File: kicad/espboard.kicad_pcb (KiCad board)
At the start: 2 copper layers, 48.3 x 40.6 mm, 14 parts, among them P1 CONN_PWR, P2 CONN_UART, P3 CONN_IO, SW1 SW_RST, SW2 SW_FLASH, U1 ESP-01v090, U2 LM1117-3.3

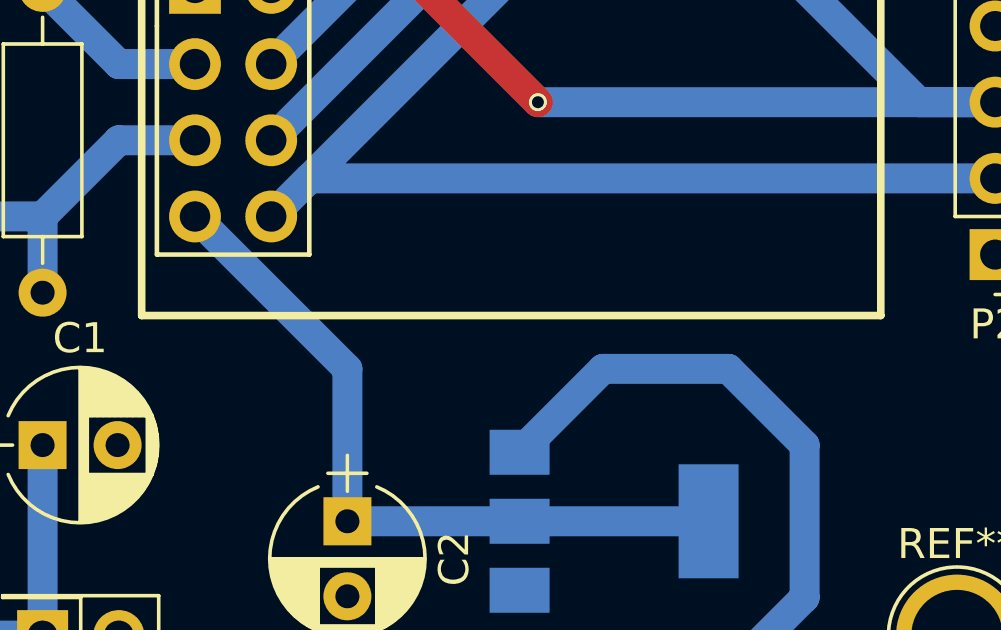
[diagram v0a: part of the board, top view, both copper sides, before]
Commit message: Fix plan de masse et ajout texte
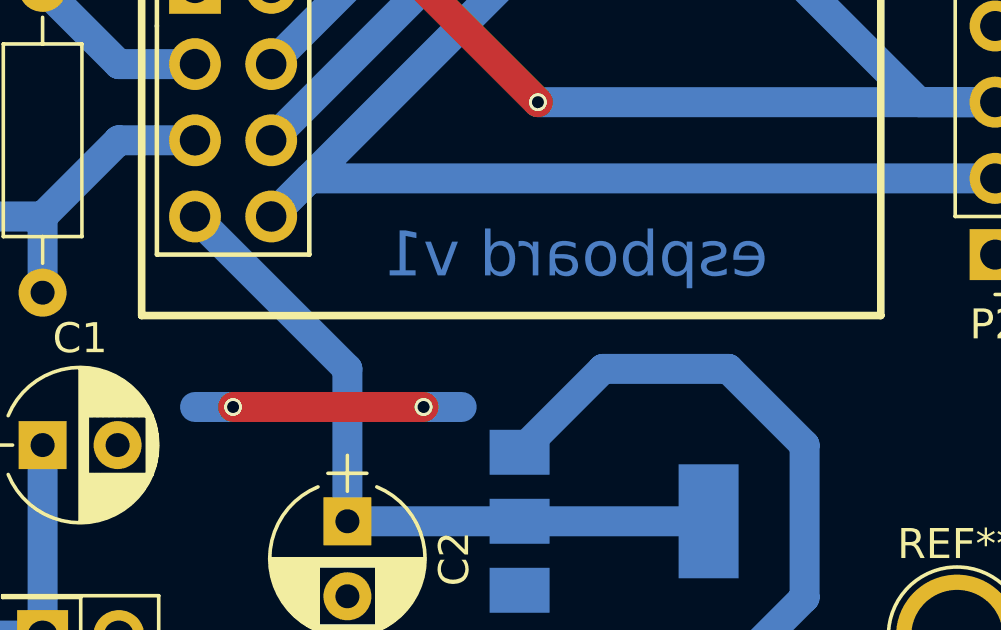
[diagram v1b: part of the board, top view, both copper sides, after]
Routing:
- net GND: track 9.78 -> 18.7 mm, vias 0 -> 2
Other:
- board text added: "espboard v1"
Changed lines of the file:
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@@
   (general
     (links 31)
-    (no_connects 2)
-    (area 130.734999 104.064999 179.145001 143.585001)
+    (no_connects 1)
+    (area 130.734999 102.794999 179.145001 143.585001)
     (thickness 1.6)
-    (drawings 6)
-    (tracks 58)
+    (drawings 7)
+    (tracks 63)
     (zones 0)
     (modules 14)
@@
       (effects (font (size 1 1) (thickness 0.15)))
     )
-    (fp_text value CONN_UART (at 0 12.49 180) (layer F.Fab)
+    (fp_text value CONN_UART (at 0 -6.35 270) (layer F.Fab)
       (effects (font (size 1 1) (thickness 0.15)))
     )
@@
       (effects (font (size 1 1) (thickness 0.15)))
     )
-    (fp_text value SW_RST (at 3.75 6.7 270) (layer F.Fab)
+    (fp_text value SW_RST (at 3.81 -2.54 270) (layer F.Fab)
       (effects (font (size 1 1) (thickness 0.15)))
     )
@@
     (fp_circle (center 0 0) (end 0 -2.286) (layer F.SilkS) (width 0.12))
     (pad 1 thru_hole circle (at 0 0) (size 4.064 4.064) (drill 3.048) (layers *.Cu *.Mask))
+  )
+  (gr_text "espboard v1" (at 162.56 127) (layer B.Cu)
+    (effects (font (size 1.5 1.5) (thickness 0.3)) (justify mirror))
   )
   (gr_line (start 130.81 102.87) (end 130.81 104.14) (angle 90) (layer Edge.Cuts) (width 0.15))
@@
   (segment (start 144.78 140.97) (end 146.05 142.24) (width 1) (layer B.Cu) (net 1))
   (segment (start 144.78 139.7) (end 144.78 133.35) (width 1) (layer B.Cu) (net 1))
+  (segment (start 149.86 132.08) (end 151.13 132.08) (width 1) (layer B.Cu) (net 2))
+  (segment (start 157.48 132.08) (end 158.75 132.08) (width 1) (layer B.Cu) (net 2))
+  (via (at 157.48 132.08) (size 0.6) (drill 0.4) (layers F.Cu B.Cu) (net 2))
+  (segment (start 151.13 132.08) (end 157.48 132.08) (width 1) (layer F.Cu) (net 2))
+  (via (at 151.13 132.08) (size 0.6) (drill 0.4) (layers F.Cu B.Cu) (net 2))
   (segment (start 152.4 118.11) (end 157.48 113.03) (width 1) (layer B.Cu) (net 2))
   (segment (start 157.48 113.03) (end 157.48 110.49) (width 1) (layer B.Cu) (net 2))

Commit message: Finalize PCB sheet
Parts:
- moved P2 68.2 mm to (115.6, 96.5)
- moved R1 68.2 mm to (83.8, 97.8)
- moved REF** 68.2 mm to (73.7, 76.2)
- moved SW1 68.2 mm to (77.5, 95.2)
- moved SW2 68.2 mm to (73.0, 89.5)
- moved U1 68.2 mm to (88.9, 87.6)
- moved C1 68.2 mm to (83.8, 102.9)
- moved C2 68.2 mm to (94.0, 105.4)
- moved P1 68.2 mm to (83.8, 109.2)
- moved P3 68.2 mm to (88.9, 80.0)
- moved REF** 68.2 mm to (114.3, 76.2)
- moved REF** 68.2 mm to (114.3, 109.2)
- moved REF** 68.2 mm to (73.7, 109.2)
- moved U2 68.2 mm to (102.9, 105.4)
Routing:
- net (no net): track 0.00 -> 8.89 mm, vias 0 -> 2
- net GND: track 18.7 -> 9.78 mm, vias 2 -> 0

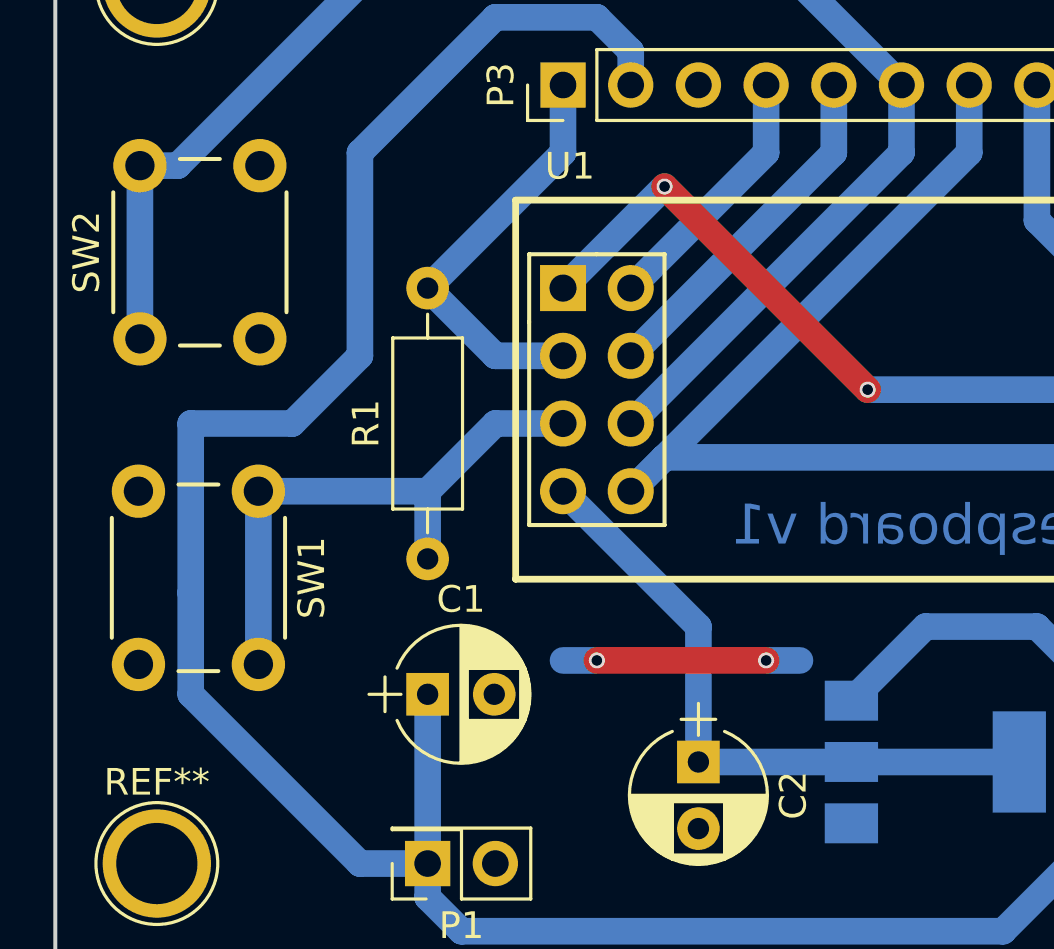
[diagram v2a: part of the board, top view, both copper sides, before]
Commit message: Bigger vias
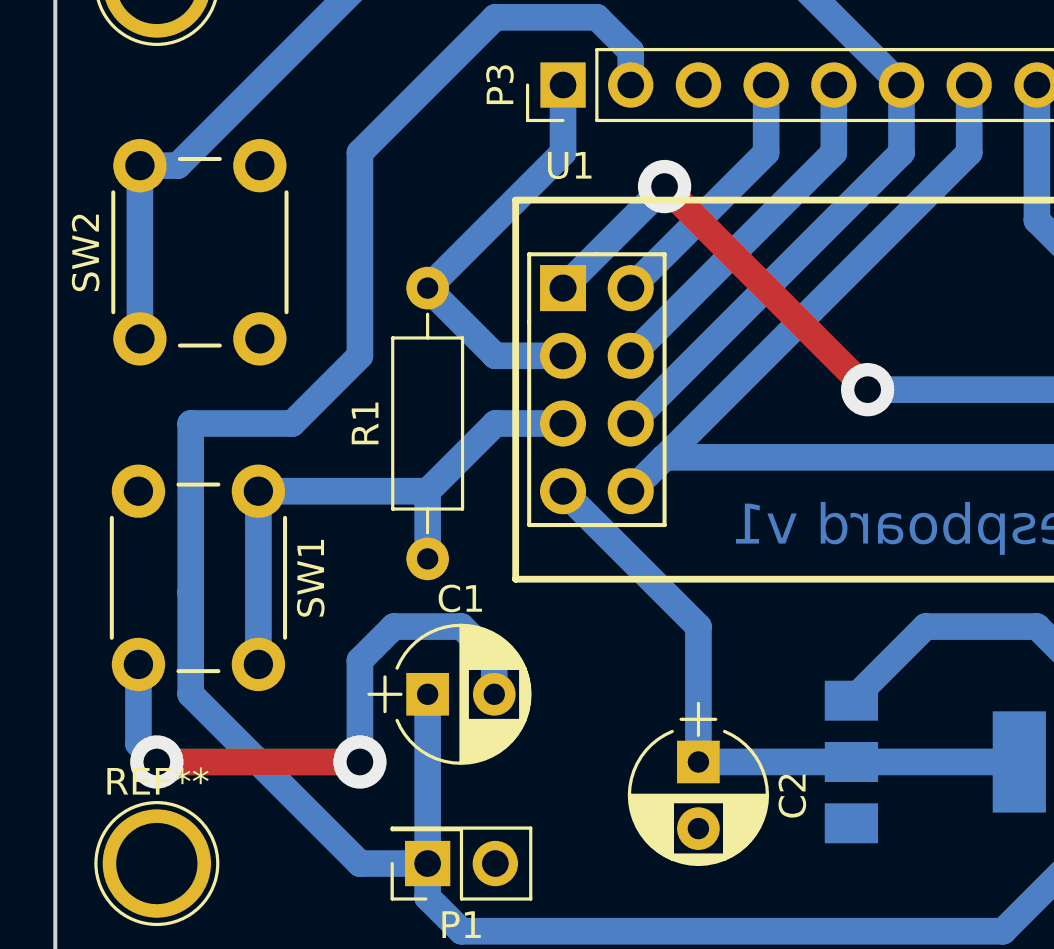
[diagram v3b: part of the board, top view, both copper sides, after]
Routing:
- net GND: track 9.78 -> 32.5 mm, vias 0 -> 2
- net (no net): track 8.89 -> 0.00 mm, vias 2 -> 0
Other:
- net class Default: via_dia 0.6 -> 2; via_drill 0.4 -> 1
- net class USB removed
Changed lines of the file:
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@@
-(kicad_pcb (version 4) (host pcbnew 4.0.5-e0-6337~49~ubuntu16.04.1)
+(kicad_pcb (version 4) (host pcbnew 4.0.5)
   (general
     (links 31)
-    (no_connects 2)
+    (no_connects 1)
     (area 69.774999 72.177 131.04 119.540001)
     (thickness 1.6)
     (drawings 9)
-    (tracks 63)
+    (tracks 68)
     (zones 0)
     (modules 14)
@@
     (segment_width 0.2)
     (edge_width 0.15)
-    (via_size 0.6)
-    (via_drill 0.4)
+    (via_size 2)
+    (via_drill 1)
     (via_min_size 0.4)
     (via_min_drill 0.3)
@@
     (clearance 0.2)
     (trace_width 1)
-    (via_dia 0.6)
-    (via_drill 0.4)
+    (via_dia 2)
+    (via_drill 1)
     (uvia_dia 0.3)
     (uvia_drill 0.1)
@@
     (add_net UART_RXD)
     (add_net UART_TXD)
-  )
-  (net_class USB ""
-    (clearance 0.2)
-    (trace_width 0.5)
-    (via_dia 0.6)
-    (via_drill 0.4)
-    (uvia_dia 0.3)
-    (uvia_drill 0.1)
   )
   (module Capacitors_THT:CP_Radial_D5.0mm_P2.50mm (layer F.Cu)
@@
   (gr_line (start 69.85 113.03) (end 69.85 73.66) (angle 90) (layer Edge.Cuts) (width 0.15))
   (gr_line (start 118.11 113.03) (end 69.85 113.03) (angle 90) (layer Edge.Cuts) (width 0.15))
-  (segment (start 88.9 101.6) (end 90.17 101.6) (width 1) (layer B.Cu) (net 0))
-  (segment (start 96.52 101.6) (end 97.79 101.6) (width 1) (layer B.Cu) (net 0))
-  (via (at 96.52 101.6) (size 0.6) (drill 0.4) (layers F.Cu B.Cu) (net 0))
-  (segment (start 90.17 101.6) (end 96.52 101.6) (width 1) (layer F.Cu) (net 0))
-  (via (at 90.17 101.6) (size 0.6) (drill 0.4) (layers F.Cu B.Cu) (net 0))
   (segment (start 91.44 80.01) (end 91.44 78.74) (width 1) (layer B.Cu) (net 1))
   (segment (start 81.28 109.22) (end 83.82 109.22) (width 1) (layer B.Cu) (net 1))
@@
   (segment (start 83.82 110.49) (end 85.09 111.76) (width 1) (layer B.Cu) (net 1))
   (segment (start 83.82 109.22) (end 83.82 102.87) (width 1) (layer B.Cu) (net 1))
+  (segment (start 86.32 102.87) (end 86.32 101.56) (width 1) (layer B.Cu) (net 2))
+  (segment (start 72.97 104.72) (end 72.97 101.75) (width 1) (layer B.Cu) (net 2))
+  (segment (start 73.66 105.41) (end 72.97 104.72) (width 1) (layer B.Cu) (net 2))
+  (via (at 73.66 105.41) (size 2) (drill 1) (layers F.Cu B.Cu) (net 2))
+  (segment (start 81.28 105.41) (end 73.66 105.41) (width 1) (layer F.Cu) (net 2))
+  (via (at 81.28 105.41) (size 2) (drill 1) (layers F.Cu B.Cu) (net 2))
+  (segment (start 81.28 101.6) (end 81.28 105.41) (width 1) (layer B.Cu) (net 2))
+  (segment (start 82.55 100.33) (end 81.28 101.6) (width 1) (layer B.Cu) (net 2))
+  (segment (start 85.09 100.33) (end 82.55 100.33) (width 1) (layer B.Cu) (net 2))
+  (segment (start 86.32 101.56) (end 85.09 100.33) (width 1) (layer B.Cu) (net 2))
   (segment (start 91.44 87.63) (end 96.52 82.55) (width 1) (layer B.Cu) (net 2))
   (segment (start 96.52 82.55) (end 96.52 80.01) (width 1) (layer B.Cu) (net 2))
@@
   (segment (start 88.9 87.63) (end 92.71 83.82) (width 1) (layer B.Cu) (net 6))
   (segment (start 100.33 91.44) (end 115.57 91.44) (width 1) (layer B.Cu) (net 6))
-  (via (at 100.33 91.44) (size 0.6) (drill 0.4) (layers F.Cu B.Cu) (net 6))
+  (via (at 100.33 91.44) (size 2) (drill 1) (layers F.Cu B.Cu) (net 6))
   (segment (start 92.71 83.82) (end 100.33 91.44) (width 1) (layer F.Cu) (net 6))
-  (via (at 92.71 83.82) (size 0.6) (drill 0.4) (layers F.Cu B.Cu) (net 6))
+  (via (at 92.71 83.82) (size 2) (drill 1) (layers F.Cu B.Cu) (net 6))
   (segment (start 115.57 91.44) (end 113.03 91.44) (width 1) (layer B.Cu) (net 6))
   (segment (start 106.68 85.09) (end 106.68 80.01) (width 1) (layer B.Cu) (net 6))

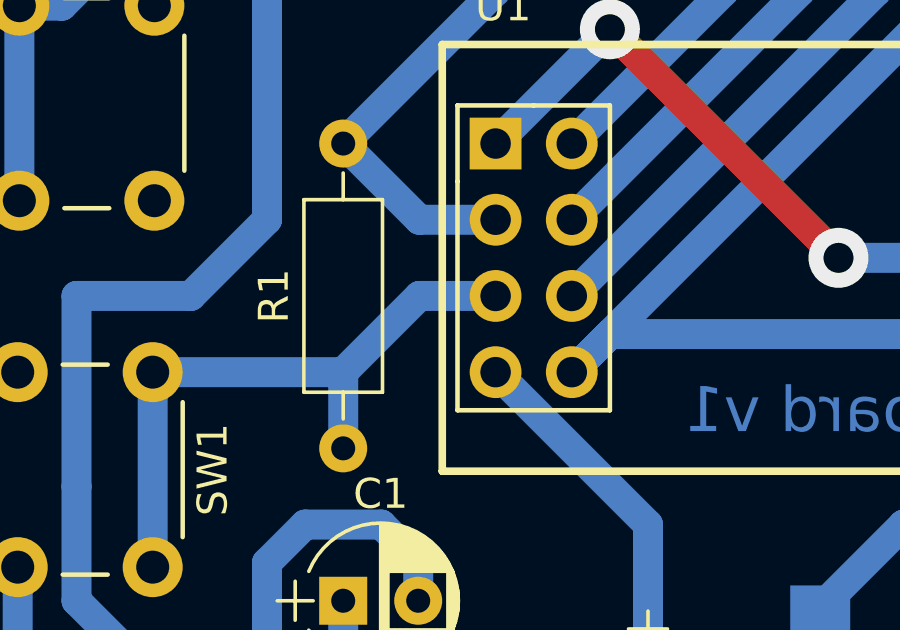
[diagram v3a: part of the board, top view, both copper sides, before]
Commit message: Fix NC for 3V3
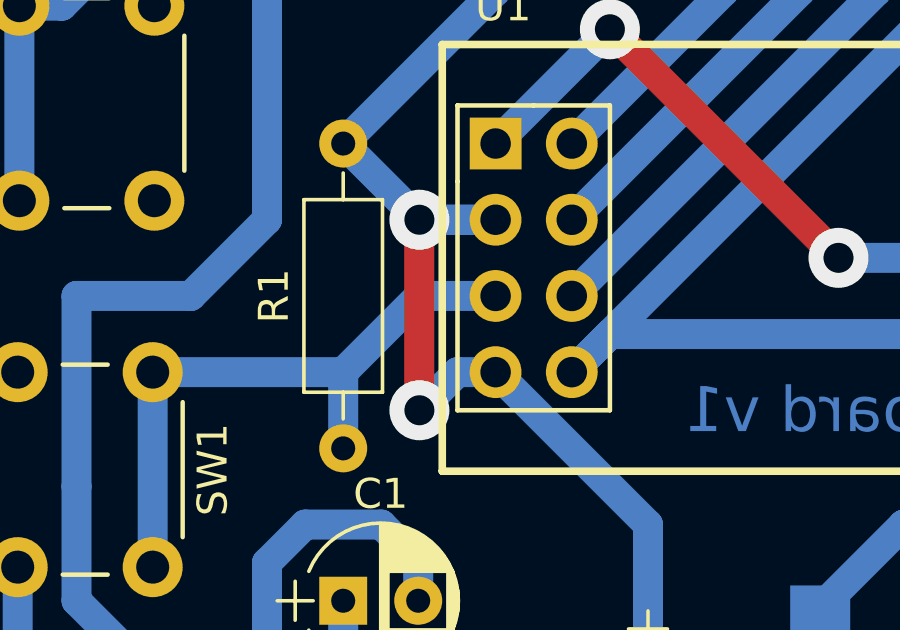
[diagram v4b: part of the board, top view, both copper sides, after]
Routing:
- net PWR_3V3: track 40.2 -> 52.1 mm, vias 0 -> 2
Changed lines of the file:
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@@
-(kicad_pcb (version 4) (host pcbnew 4.0.5)
+(kicad_pcb (version 4) (host pcbnew 4.0.5-e0-6337~49~ubuntu16.04.1)
   (general
     (links 31)
-    (no_connects 1)
-    (area 69.774999 72.177 131.04 119.540001)
+    (no_connects 0)
+    (area 69.774999 72.314999 118.185001 113.105001)
     (thickness 1.6)
     (drawings 9)
-    (tracks 68)
+    (tracks 74)
     (zones 0)
     (modules 14)
@@
   (segment (start 96.52 82.55) (end 96.52 80.01) (width 1) (layer B.Cu) (net 2))
   (segment (start 86.36 102.91) (end 86.32 102.87) (width 1) (layer B.Cu) (net 2))
+  (segment (start 88.9 95.25) (end 87.63 95.25) (width 1) (layer B.Cu) (net 3))
+  (via (at 86.36 90.17) (size 2) (drill 1) (layers F.Cu B.Cu) (net 3))
+  (segment (start 86.36 96.52) (end 86.36 90.17) (width 1) (layer F.Cu) (net 3))
+  (via (at 86.36 96.52) (size 2) (drill 1) (layers F.Cu B.Cu) (net 3))
+  (segment (start 87.63 95.25) (end 86.36 96.52) (width 1) (layer B.Cu) (net 3))
+  (segment (start 86.36 90.17) (end 88.9 90.17) (width 1) (layer B.Cu) (net 3))
   (segment (start 83.82 87.63) (end 86.36 90.17) (width 1) (layer B.Cu) (net 3))
   (segment (start 86.36 90.17) (end 88.9 90.17) (width 1) (layer B.Cu) (net 3))

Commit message: v2
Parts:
- removed the REF** at (114.3, 76.2)
- removed the REF** at (114.3, 109.2)
- removed the REF** at (73.7, 109.2)
- removed the REF** at (73.7, 76.2)
- removed SW1: SW_RST, Buttons_Switches_THT:SW_PUSH_6mm
- removed SW2: SW_FLASH, Buttons_Switches_THT:SW_PUSH_6mm
- added FLASH: SW_FLASH, Buttons_Switches_THT:SW_PUSH_6mm, F.Cu at (166.4, 99.1)
- added J1: USB_OTG, Connectors:USB_Micro-B, B.Cu at (152.4, 96.5)
- added P4: usb_connector, usb_connector:usb_adapter, F.Cu at (158.8, 96.5)
- added REF**: 1pin, Connectors:1pin, F.Cu at (209.6, 82.5)
- added REF**: 1pin, Connectors:1pin, F.Cu at (209.6, 115.6)
- added REF**: 1pin, Connectors:1pin, F.Cu at (151.1, 115.6)
- added REF**: 1pin, Connectors:1pin, F.Cu at (151.1, 82.5)
- added REF***: OSHW-Logo2_14.6x12mm_SilkScreen, Symbols:OSHW-Logo2_14.6x12mm_SilkScreen, F.Cu at (200.7, 97.8)
- added RST: SW_RST, Buttons_Switches_THT:SW_PUSH_6mm, F.Cu at (166.4, 88.9)
- P1: value CONN_PWR -> ftdi; footprint Socket_Strips:Socket_Strip_Straight_2x01_Pitch2.54mm -> Pin_Headers:Pin_Header_Straight_1x06_Pitch2.54mm
- P2: value CONN_UART -> CONN_PWR; footprint Socket_Strips:Socket_Strip_Straight_1x05_Pitch2.54mm -> Socket_Strips:Socket_Strip_Straight_2x01_Pitch2.54mm
- moved P1 101.6 mm to (185.4, 109.2), turned to 90 degrees
- moved U1 96.7 mm to (185.4, 94.0)
- moved P3 96.7 mm to (185.4, 86.4)
- moved R1 94.4 mm to (177.8, 88.9), turned to 270 degrees
- moved C2 82.6 mm to (176.5, 108.0)
- moved C1 75.1 mm to (158.8, 108.0), turned to 270 degrees
- moved U2 65.0 mm to (167.6, 110.5)
- moved P2 37.4 mm to (151.1, 108.0), turned to 90 degrees
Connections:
- P1 pad 1: PWR_5V -> GND
- P1 pad 2: GND -> Net-(P1-Pad2)
- P2 pad 1: Net-(P2-Pad1) -> PWR_5V
- P2 pad 2: UART_TXD -> GND
- P3 pad 1: PWR_3V3 -> PWR_5V
- P3 pad 2: PWR_5V -> PWR_3V3
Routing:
- net PWR_5V: track 102.7 -> 75.1 mm
- net UART_TXD: track 45.2 -> 30.2 mm
- net UART_RXD: track 48.0 -> 61.4 mm, vias 2 -> 0
- net PWR_3V3: track 52.1 -> 59.6 mm, vias 2 -> 0
- net ESP_GPIO0: track 57.4 -> 50.3 mm
- net GND: track 32.5 -> 26.2 mm, vias 2 -> 0
- net Net-(R1-Pad1): track 21.4 -> 24.7 mm
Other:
- board size 48.3 x 40.6 mm -> 66 x 40.6 mm
- net class Default: trace_width 1 -> 0.4; via_dia 2 -> 0.4; via_drill 1 -> 0.3
- net class Power added: clearance 0.2, trace_width 1, via_dia 0.4, via_drill 0.3
- board text added: "espboard v2"
- board text removed: "espboard v1"
